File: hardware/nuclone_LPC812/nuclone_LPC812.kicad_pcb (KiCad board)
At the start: 2 copper layers, 2 parts

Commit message: initial PCB layout
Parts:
- added C1: 100n, SquantorRcl:C_0805, F.Cu at (99.4, 63.6)
- added C2: 10u, SquantorRcl:C_0603, F.Cu at (99.2, 69.2)
- added F1: 0.5A, SquantorRcl:F_0603_hand, F.Cu at (99.2, 67.7)
- added FB1: 100, SquantorRcl:L_0603, F.Cu at (96.4, 67.7)
- added H1: MountingHole, MountingHole:MountingHole_3.2mm_M3_Pad_Via, F.Cu at (64.8, 64.8)
- added H2: MountingHole, MountingHole:MountingHole_3.2mm_M3_Pad_Via, F.Cu at (105.4, 64.8)
- added H3: MountingHole, MountingHole:MountingHole_3.2mm_M3_Pad_Via, F.Cu at (105.4, 105.4)
- added H4: MountingHole, MountingHole:MountingHole_3.2mm_M3_Pad_Via, F.Cu at (64.8, 105.4)
- added J1: JTAG_2X05, SquantorConnectors:Header-0127-2X05-H006, F.Cu at (76.2, 63.5)
- added J2: USB-ID, SquantorUsb:USB-muB-SMD_TH, F.Cu at (92.7, 63.7)
- added J3: PINS_2X10, SquantorConnectors:Header-0254-2X10-H010, F.Cu at (66.0, 86.4)
- added J4: PINS_2X10, SquantorConnectors:Header-0254-2X10-H010, F.Cu at (104.1, 86.4)
- added R1: 100K, SquantorRcl:R_0402_hand, F.Cu at (78.8, 68.6)
- added R10: 100, SquantorRcl:R_0402_hand, F.Cu at (73.6, 66.3)
- added R11: 0, SquantorRcl:R_0603_hand, F.Cu at (89.3, 68.3)
- added R2: 100k, SquantorRcl:R_0402_hand, F.Cu at (77.5, 68.6)
- added R3: 100k, SquantorRcl:R_0402_hand, F.Cu at (76.2, 68.6)
- added R4: 100K, SquantorRcl:R_0402_hand, F.Cu at (74.9, 68.6)
- added R5: 100k, SquantorRcl:R_0402_hand, F.Cu at (73.6, 68.6)
- added R6: 100, SquantorRcl:R_0402_hand, F.Cu at (78.8, 66.3)
- added R7: 100, SquantorRcl:R_0402_hand, F.Cu at (77.5, 66.3)
- added R8: 100, SquantorRcl:R_0402_hand, F.Cu at (76.2, 66.3)
- added R9: 100, SquantorRcl:R_0402_hand, F.Cu at (74.9, 66.3)
- added U1: USBLC6-2, SquantorIC:SOT23-6-HAND, F.Cu at (93.0, 69.6)
- N1: moved to B.Cu
- N2: value V20180719 -> 20180828; moved to B.Cu
- moved N2 66.3 mm to (83.2, 91.0)
- moved N1 64.8 mm to (84.7, 87.0), turned to 180 degrees
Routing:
- net Net-(C1-Pad1): track 0.00 -> 16.2 mm
- net /VSS: track 0.00 -> 7.00 mm, vias 0 -> 2
- net Net-(J2-Pad4): track 0.00 -> 4.32 mm
- added copper zone on B.Cu, net /VSS
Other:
- board outline added: 48.3 x 48.3 mm

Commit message: added psu components
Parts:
- added C4: 10u, SquantorRcl:C_0603, F.Cu at (97.8, 77.8)
- added U2: MCP1702-MB, SquantorIC:SOT89-SOT23-Dual-NXP, F.Cu at (98.1, 72.7)
- moved C2 3.41 mm to (102.6, 69.4), turned to 0 degrees
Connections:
- net /Jtag connector/RESET renamed /MCU_RESET
- net /Jtag connector/TCK renamed /MCU_TCK
- net /Jtag connector/TDO renamed /MCU_TDO
- net /Jtag connector/TMS renamed /MCU_TMS

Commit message: further layout bits
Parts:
- N2: value 20180828 -> 20180918
- R1, R10, R2, R3, R4, R5, R6, R7, R8, R9: footprint SquantorRcl:R_0402_hand -> SquantorRcl:R_0603_hand
- moved R1 1.08 mm to (79.2, 69.6)
- moved R5 1.08 mm to (73.2, 69.6)
- moved R2 1.02 mm to (77.7, 69.6)
- moved R4 1.02 mm to (74.7, 69.6)
- moved R3 1.00 mm to (76.2, 69.6)
- moved R6 0.57 mm to (79.2, 66.7)
- moved R10 0.57 mm to (73.2, 66.7)
- moved R7 0.45 mm to (77.7, 66.7)
- moved R9 0.45 mm to (74.7, 66.7)
- moved R8 0.40 mm to (76.2, 66.7)
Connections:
- net Net-(J2-Pad2) renamed /USB input/USB_IN_D-
- net Net-(J2-Pad3) renamed /USB input/USB_IN_D+
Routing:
- net /VBUS: track 0.00 -> 11.6 mm
- net Net-(FB1-Pad2): track 0.00 -> 4.08 mm
- net /USB input/USB_IN_D+: track 0.00 -> 3.76 mm
- net /USB input/USB_IN_D-: track 0.00 -> 3.73 mm
- net /VSS: track 7.00 -> 8.96 mm, vias 2 -> 3
- net Net-(F1-Pad2): track 0.00 -> 1.30 mm

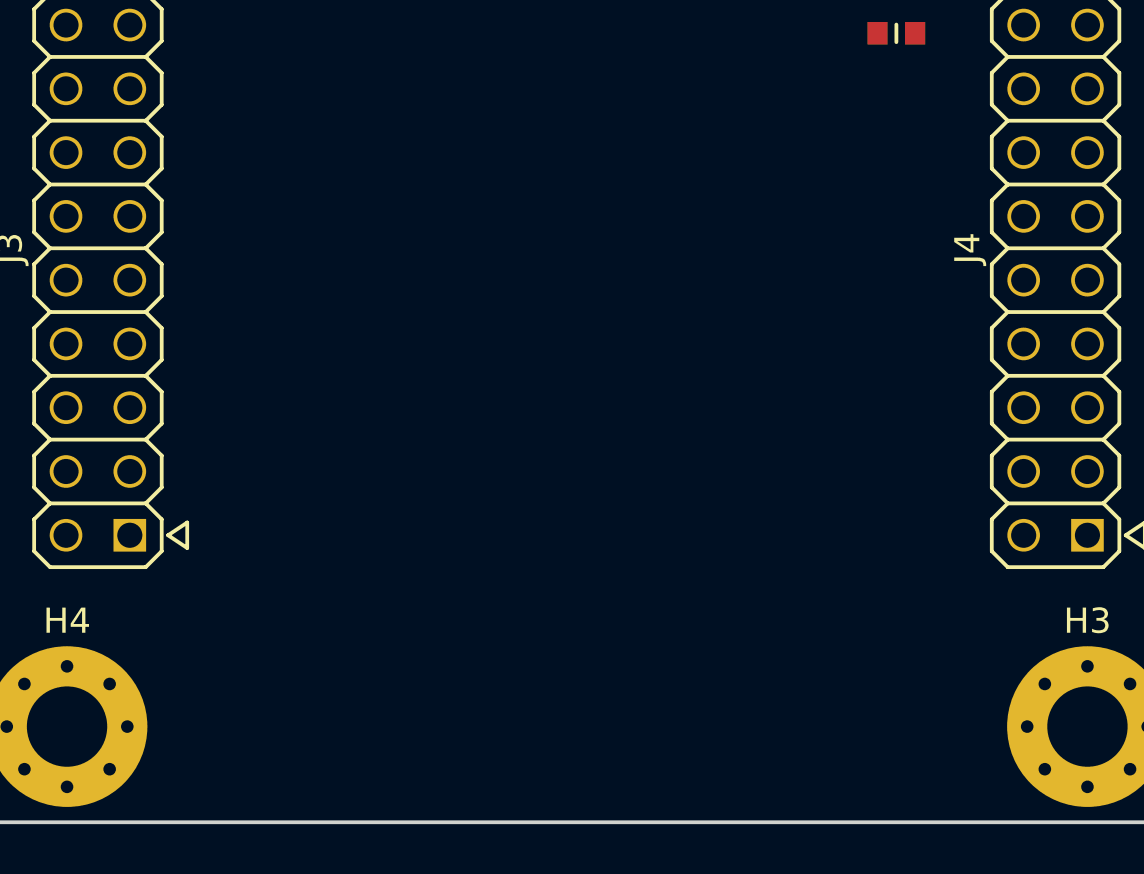
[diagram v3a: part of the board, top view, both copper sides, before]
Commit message: component placement
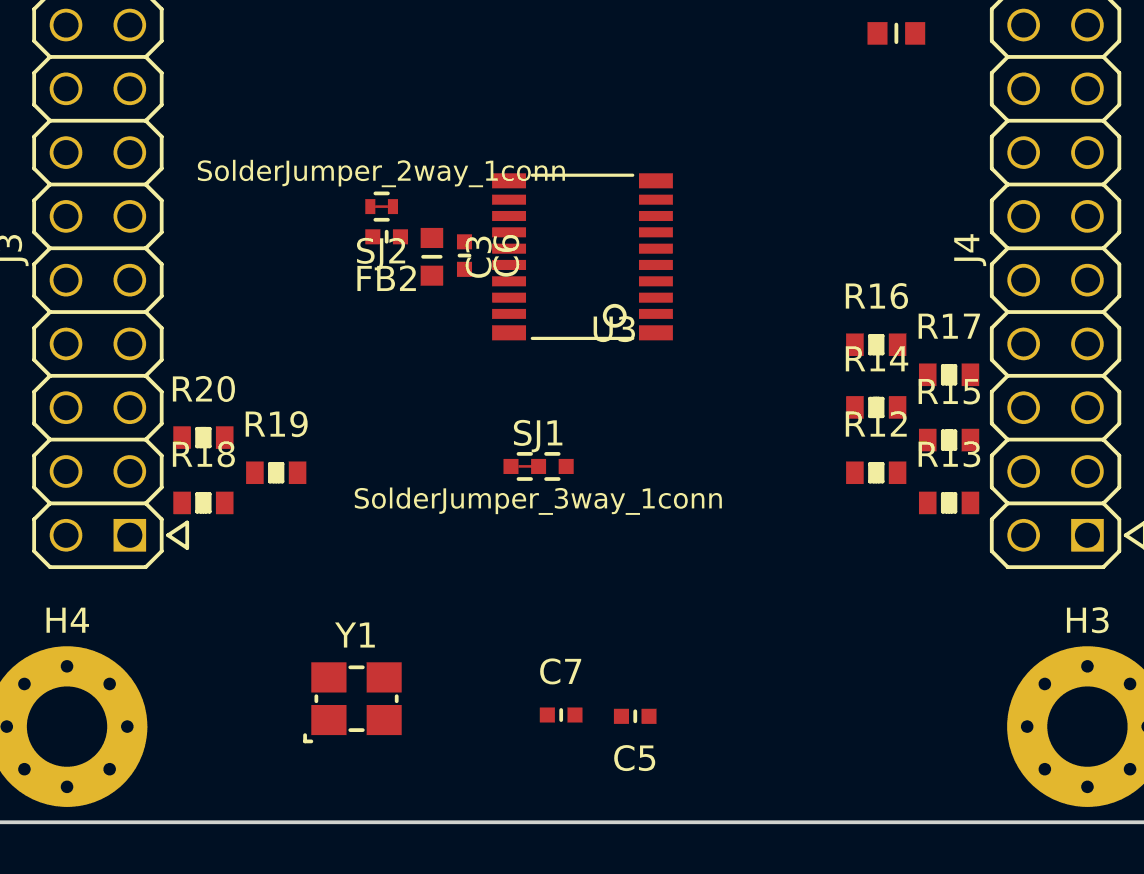
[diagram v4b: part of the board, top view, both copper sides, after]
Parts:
- added C3: 10u, SquantorRcl:C_0603, F.Cu at (79.3, 86.7)
- added C5: 18p, SquantorRcl:C_0402, F.Cu at (87.4, 105.0)
- added C6: 1u, SquantorRcl:C_0402, F.Cu at (80.6, 86.7)
- added C7: 18p, SquantorRcl:C_0402, F.Cu at (84.5, 105.0)
- added FB2: FB, SquantorRcl:C_0402, F.Cu at (77.5, 85.9)
- added R12: 100, SquantorRcl:R_0603_hand, F.Cu at (97.0, 95.3)
- added R13: 100, SquantorRcl:R_0603_hand, F.Cu at (99.9, 96.5)
- added R14: 100, SquantorRcl:R_0603_hand, F.Cu at (97.0, 92.7)
- added R15: 100, SquantorRcl:R_0603_hand, F.Cu at (99.9, 94.0)
- added R16: 100, SquantorRcl:R_0603_hand, F.Cu at (97.0, 90.2)
- added R17: 100, SquantorRcl:R_0603_hand, F.Cu at (99.9, 91.4)
- added R18: 100, SquantorRcl:R_0603_hand, F.Cu at (70.2, 96.5)
- added R19: 100, SquantorRcl:R_0603_hand, F.Cu at (73.1, 95.3)
- added R20: 100, SquantorRcl:R_0603_hand, F.Cu at (70.2, 93.9)
- added SJ1: SolderJumper_3way_1conn, SquantorSpecial:solder_jumper_3way_12conn, F.Cu at (83.5, 95.0)
- added SJ2: SolderJumper_2way_1conn, SquantorSpecial:solder_jumper_2way_conn, F.Cu at (77.3, 84.7)
- added U3: LPC812M101JDH20, SquantorIC:SOT360, F.Cu at (85.3, 86.7)
- added Y1: 12MHz, SquantorCrystal:Crystal_3225_4, F.Cu at (76.3, 104.3)
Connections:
- net /VSS renamed VSS
- J3 pad 3: (no net) -> /GPIO_01
- J3 pad 4: (no net) -> /GPIO_00
- J3 pad 6: (no net) -> /GPIO_02
- J4 pad 13: (no net) -> /AN_00
- J4 pad 14: (no net) -> /VREF
- J4 pad 16: (no net) -> /AN_01
- J4 pad 3: (no net) -> /I2C_SCL
- J4 pad 4: (no net) -> /I2C_SDA
- J4 pad 5: (no net) -> /SPI_MISO
- J4 pad 6: (no net) -> /SPI_MOSI
- J4 pad 7: (no net) -> /SPI_CE
- J4 pad 8: (no net) -> /SPI_SCLK

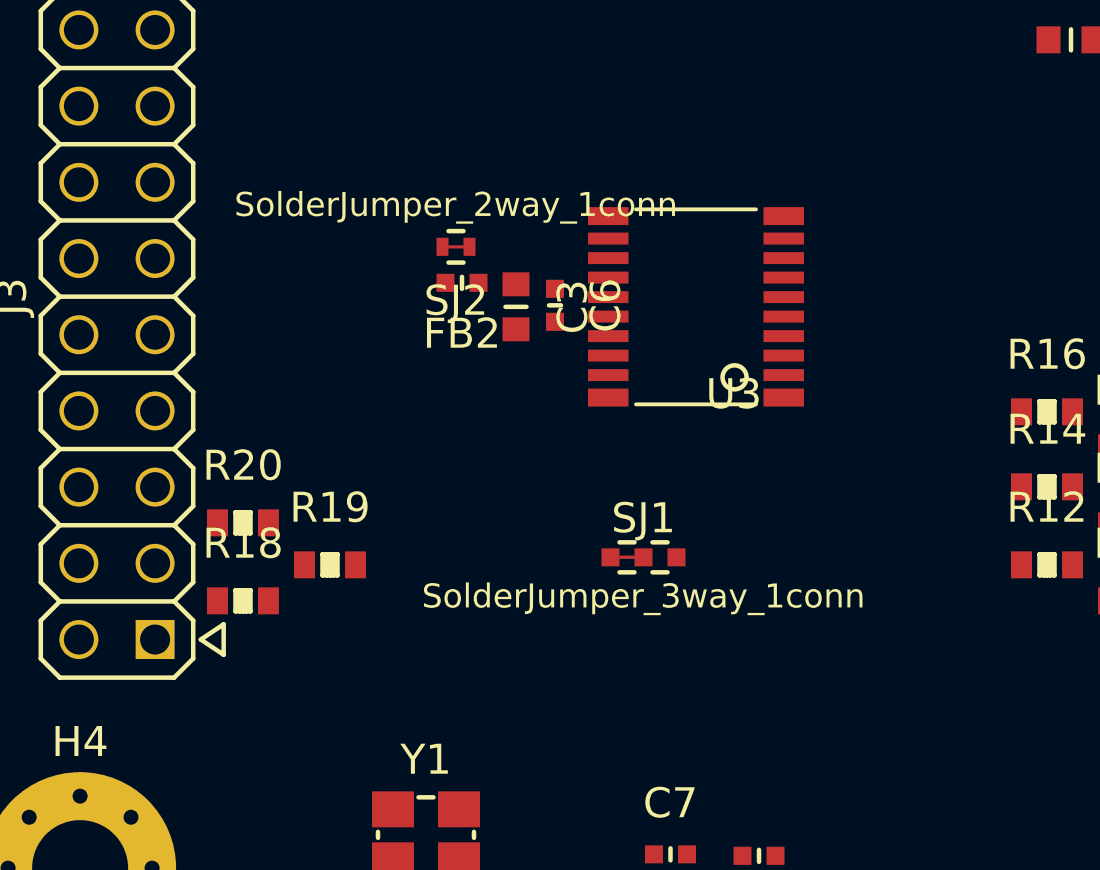
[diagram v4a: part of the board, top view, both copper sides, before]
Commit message: imported components on the PCB
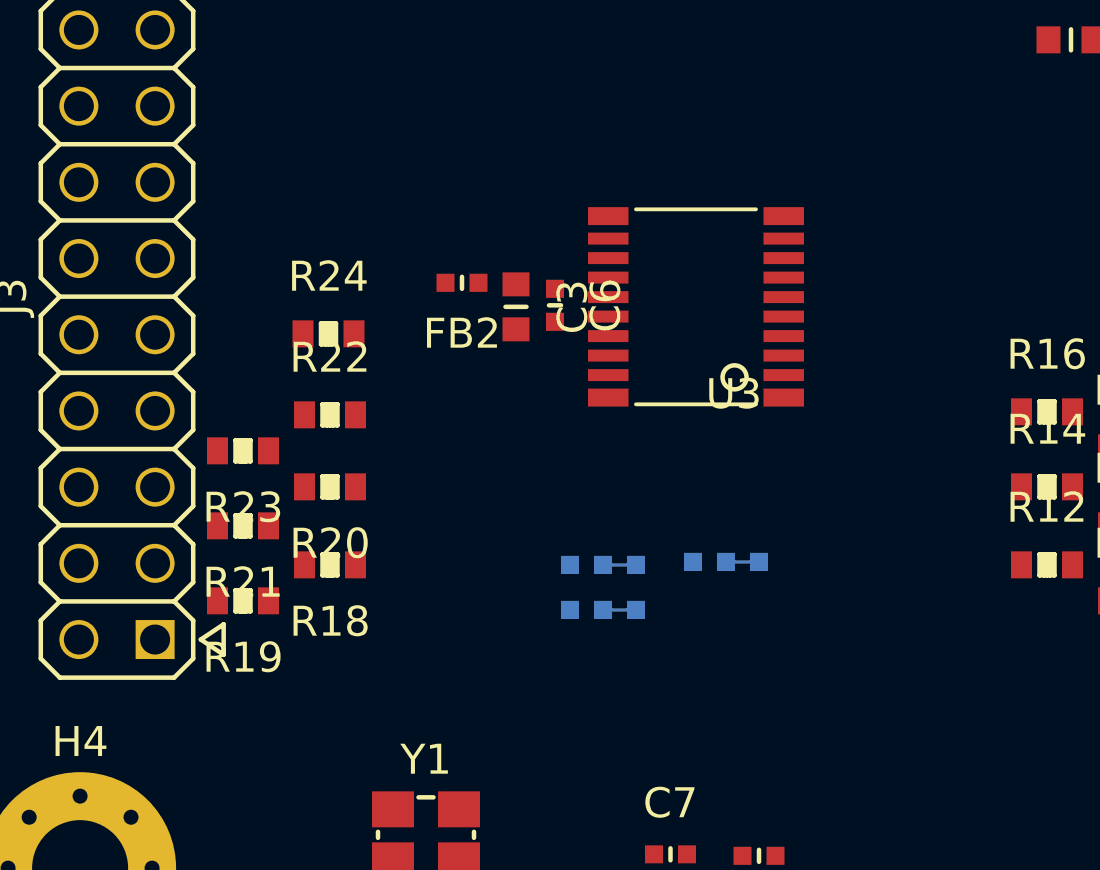
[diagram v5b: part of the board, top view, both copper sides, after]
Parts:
- removed SJ1: SolderJumper_3way_1conn, SquantorSpecial:solder_jumper_3way_12conn
- removed SJ2: SolderJumper_2way_1conn, SquantorSpecial:solder_jumper_2way_conn
- added JP1: RESET/GPIO, SquantorSpecial:solder_jumper_3way_23conn, B.Cu at (82.2, 95.3)
- added JP2: XTAL/GPIO, SquantorSpecial:solder_jumper_3way_23conn, B.Cu at (82.2, 96.8)
- added JP3: XTAL/GPIO, SquantorSpecial:solder_jumper_3way_23conn, B.Cu at (86.3, 95.2)
- added R21: 100, SquantorRcl:R_0603_hand, F.Cu at (70.2, 94.0)
- added R22: 100, SquantorRcl:R_0603_hand, F.Cu at (73.1, 90.3)
- added R23: 100, SquantorRcl:R_0603_hand, F.Cu at (70.2, 91.5)
- added R24: 100, SquantorRcl:R_0603_hand, F.Cu at (73.0, 87.6)
- J3, J4: value PINS_2X10 -> Conn_02x10_Odd_Even
- moved R18 3.14 mm to (73.1, 95.3), turned to 180 degrees
- moved R19 3.14 mm to (70.2, 96.5), turned to 180 degrees
- moved R20 3.14 mm to (73.1, 92.7), turned to 180 degrees
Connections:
- C5 pad 1: /LPC812M101JD20 base/PIO0_9 -> /LPC812M101JD20 base/XTAL_IN
- C7 pad 1: /LPC812M101JD20 base/PIO0_8 -> /LPC812M101JD20 base/XTAL_OUT
- FB2 pad 2: Net-(FB2-Pad2) -> /VDD
- J3 pad 3: /GPIO_01 -> /GPIO_00
- J3 pad 4: /GPIO_00 -> /GPIO_01
- J3 pad 5: (no net) -> /GPIO_02
- J3 pad 6: /GPIO_02 -> /GPIO_03
- J3 pad 7: (no net) -> /GPIO_04
- J3 pad 8: (no net) -> /GPIO_05
- J3 pad 9: (no net) -> /GPIO_06
- J4 pad 13: /AN_00 -> /VREF
- J4 pad 14: /VREF -> /AN_00
- J4 pad 15: (no net) -> /AN_01
- J4 pad 16: /AN_01 -> (no net)
- J4 pad 3: /I2C_SCL -> /I2C_SDA
- J4 pad 4: /I2C_SDA -> /I2C_SCL
- J4 pad 5: /SPI_MISO -> /SPI_MOSI
- J4 pad 6: /SPI_MOSI -> /SPI_MISO
- J4 pad 7: /SPI_CE -> /SPI_SCLK
- J4 pad 8: /SPI_SCLK -> /SPI_CE
- R14 pad 1: (no net) -> /LPC812M101JD20 base/PIO0_17
- R15 pad 1: (no net) -> /LPC812M101JD20 base/PIO0_13
- R16 pad 1: (no net) -> /LPC812M101JD20 base/PIO0_12
- R17 pad 1: (no net) -> /LPC812M101JD20 base/PIO0_4
- R18 pad 1: /GPIO_00 -> /LPC812M101JD20 base/PIO0_7
- R19 pad 1: /GPIO_01 -> /LPC812M101JD20 base/PIO0_14
- R20 pad 1: /GPIO_02 -> /LPC812M101JD20 base/PIO0_15
- U3 pad 1: (no net) -> /LPC812M101JD20 base/PIO0_17
- U3 pad 10: (no net) -> /LPC812M101JD20 base/PIO0_16
- U3 pad 11: (no net) -> /LPC812M101JD20 base/PIO0_15
- U3 pad 17: (no net) -> /LPC812M101JD20 base/PIO0_7
- U3 pad 2: (no net) -> /LPC812M101JD20 base/PIO0_13
- U3 pad 20: (no net) -> /LPC812M101JD20 base/PIO0_14
- U3 pad 3: (no net) -> /LPC812M101JD20 base/PIO0_12
- U3 pad 4: (no net) -> /LPC812M101JD20 base/PIO0_5
- U3 pad 5: (no net) -> /LPC812M101JD20 base/PIO0_4
- U3 pad 6: (no net) -> /MCU_TCK
- U3 pad 7: (no net) -> /MCU_TMS
- Y1 pad 1: /LPC812M101JD20 base/PIO0_9 -> /LPC812M101JD20 base/XTAL_IN
- Y1 pad 3: /LPC812M101JD20 base/PIO0_8 -> /LPC812M101JD20 base/XTAL_OUT

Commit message: further component placement
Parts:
- R1, R10, R11, R12, R13, R14, R15, R16, R17, R18, R19, R2, R20, R21, R22, R23, R24, R3, R4, R5, R6, R7, R8, R9: footprint SquantorRcl:R_0603_hand -> SquantorRcl:R_0402_hand
- moved C7 27.6 mm to (76.5, 78.5)
- moved C5 27.4 mm to (84.0, 77.8)
- moved Y1 25.3 mm to (79.8, 79.2)
- moved JP3 14.3 mm to (78.9, 83.0)
- moved JP2 12.9 mm to (78.9, 84.3)
- moved JP1 12.0 mm to (91.6, 87.9)
- moved R14 3.18 mm to (99.9, 94.0)
- moved R16 3.16 mm to (99.9, 91.5)
- moved R12 3.14 mm to (99.9, 96.5)
- moved R6 3.07 mm to (76.1, 66.9)
- moved R1 3.07 mm to (76.1, 69.4)
- moved R22 2.90 mm to (70.2, 90.2), turned to 180 degrees
- moved R18 2.90 mm to (70.2, 95.2)
- moved R20 2.90 mm to (70.2, 92.7)
- moved R7 2.84 mm to (74.9, 66.9)
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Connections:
- JP1 pad 1: /GPIO_04 -> /LPC812M101JD20 base/GPIO_04_INT
- JP2 pad 1: /GPIO_05 -> /LPC812M101JD20 base/GPIO_05_INT
- JP3 pad 1: /GPIO_06 -> /LPC812M101JD20 base/GPIO_06_INT
- R22 pad 1: /GPIO_04 -> /LPC812M101JD20 base/GPIO_04_INT
- R23 pad 1: /GPIO_05 -> /LPC812M101JD20 base/GPIO_05_INT
- R24 pad 1: /GPIO_06 -> /LPC812M101JD20 base/GPIO_06_INT

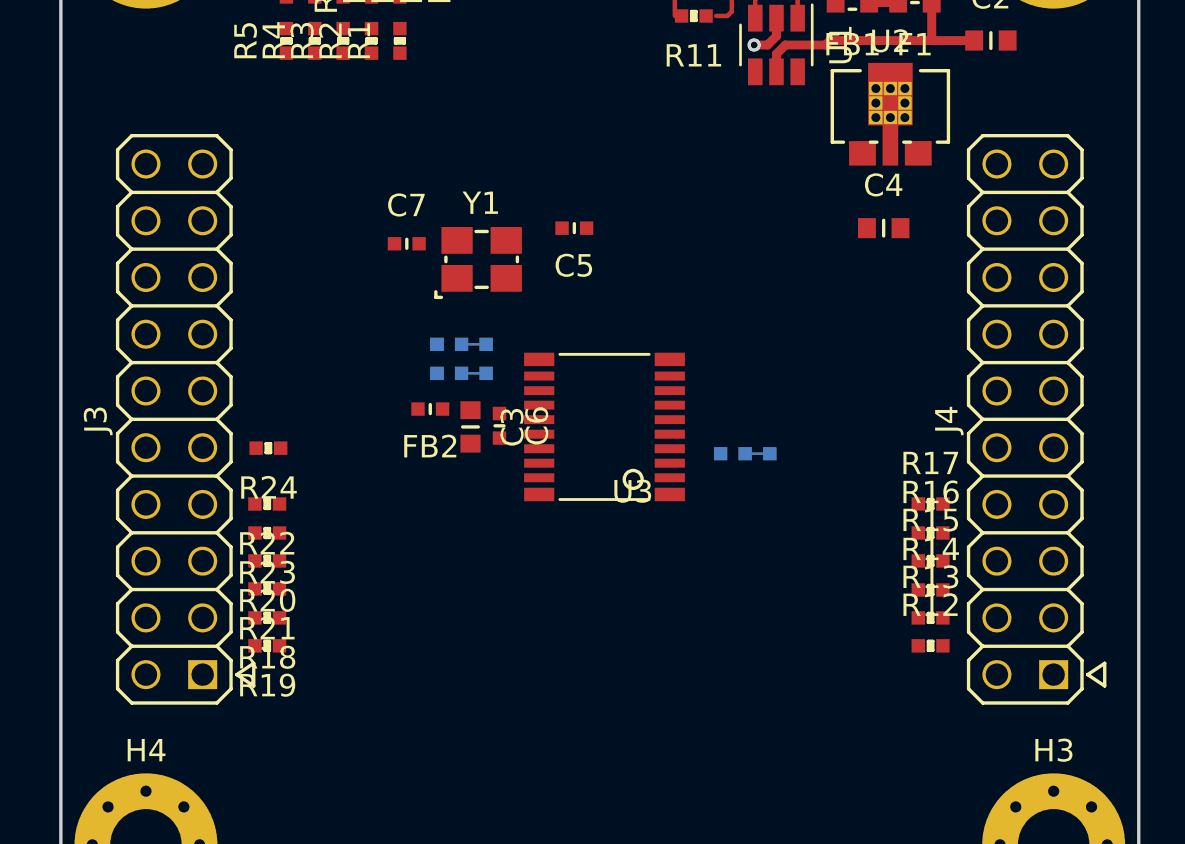
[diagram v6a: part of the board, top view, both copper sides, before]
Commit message: updated named connectors
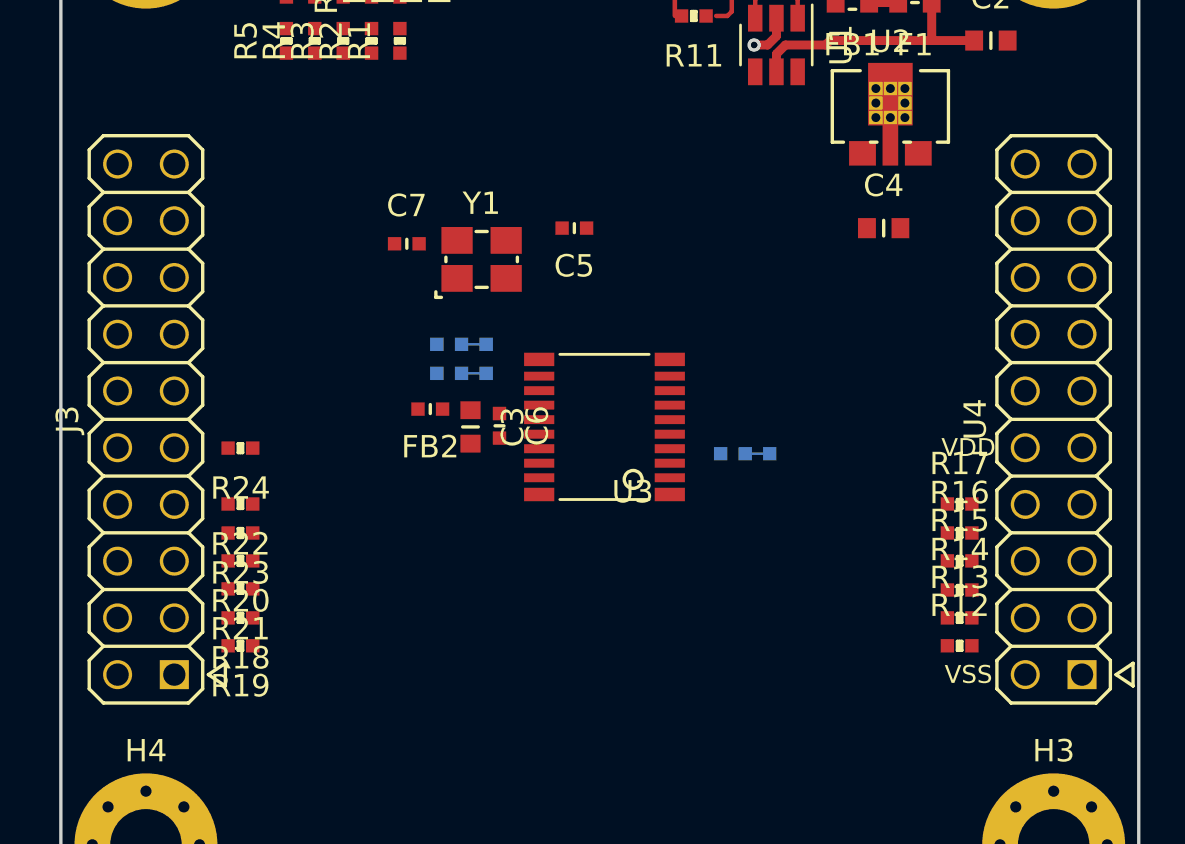
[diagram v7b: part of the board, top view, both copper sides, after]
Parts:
- removed J4: Conn_02x10_Odd_Even, SquantorConnectors:Header-0254-2X10-H010
- added U4: nuclone_20pin_bus_analog, SquantorConnectorsNamed:Nuclone_20pin_bus_analog, F.Cu at (105.4, 86.4)
- J3: value Conn_02x10_Odd_Even -> nuclone_20pin_gpio; footprint SquantorConnectors:Header-0254-2X10-H010 -> SquantorConnectorsNamed:Nuclone_20pin_gpio
- moved R12 1.30 mm to (101.2, 96.5)
- moved R13 1.30 mm to (101.2, 95.2)
- moved R14 1.30 mm to (101.2, 94.0)
- moved R15 1.30 mm to (101.2, 92.7)
- moved R16 1.30 mm to (101.2, 91.5)
- moved R17 1.30 mm to (101.2, 90.2)
- moved J3 1.27 mm to (64.8, 86.4)
- moved R24 1.25 mm to (69.0, 87.7)
- moved R18 1.20 mm to (69.0, 95.2)
- moved R19 1.20 mm to (69.0, 96.5)
- moved R20 1.20 mm to (69.0, 92.7)
- moved R21 1.20 mm to (69.0, 94.0)
- moved R22 1.20 mm to (69.0, 90.2)
- moved R23 1.20 mm to (69.0, 91.5)
